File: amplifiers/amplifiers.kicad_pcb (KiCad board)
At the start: 2 copper layers, 4 parts, among them J1 Conn_01x03_Pin, J2 Conn_01x02_Pin, J3 Conn_01x03_Pin, U1 ADA4898-2

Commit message: Finishes version 0.1 of amplifier module board
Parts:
- moved J3 6.73 mm to (151.0, 88.9)
- moved U1 5.35 mm to (143.9, 91.9)
- moved J2 4.92 mm to (142.7, 86.0)
- moved J1 4.61 mm to (137.0, 94.0)
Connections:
- U1 pad 5: Net-(J3-Pin_2) -> Net-(J3-Pin_3)
- U1 pad 6: Net-(J3-Pin_3) -> Net-(J3-Pin_2)
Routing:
- net Net-(J2-Pin_2): track 0.00 -> 9.89 mm
- net VEE: track 0.00 -> 8.55 mm
- net VDD: track 0.00 -> 7.54 mm, vias 0 -> 1
- net Net-(J1-Pin_3): track 0.00 -> 5.98 mm
- net Net-(J3-Pin_2): track 0.00 -> 5.07 mm
- net Net-(J1-Pin_2): track 0.00 -> 4.87 mm
- net Net-(J3-Pin_3): track 0.00 -> 4.70 mm
- net Net-(J2-Pin_1): track 0.00 -> 4.54 mm
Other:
- board outline added: 18 x 14 mm
- board text added: "+In1"
- board text added: "+In2"
- board text added: "+Vs"
- board text added: "-In1"
- board text added: "-In2"
- board text added: "-Vs"
- board text added: "Analog Amplifier"
- board text added: "Vo1"
- board text added: "Vo2"
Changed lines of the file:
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@@
   )
   (paper "A4")
+  (title_block
+    (title "Analog Amplifier Module Board PCB")
+    (date "2024-02-07")
+    (rev "0.1")
+    (company "Carlos Craveiro")
+    (comment 1 "Part of the Eibstein-Boltzmann Project")
+  )
   (layers
     (0 "F.Cu" signal)
@@
   (net 8 "Net-(J3-Pin_3)")
   (footprint "Package_SO:SOIC-8-1EP_3.9x4.9mm_P1.27mm_EP2.41x3.81mm" (layer "F.Cu")
-    (at 148.525 94.595)
+    (at 143.9 91.905)
     (descr "SOIC, 8 Pin (https://www.analog.com/media/en/technical-documentation/data-sheets/ada4898-1_4898-2.pdf#page=29), generated with kicad-footprint-generator ipc_gullwing_generator.py")
     (tags "SOIC SO")
@@
     (attr smd)
     (fp_text reference "U1" (at 0 -3.4) (layer "F.SilkS")
-        (effects (font (size 1 1) (thickness 0.15)))
+        (effects (font (size 1 1) (thickness 0.2) bold))
     )
     (fp_text value "ADA4898-2" (at 0 3.4) (layer "F.Fab")
@@
       (net 1 "VEE") (pinfunction "V-") (pintype "power_in"))
     (pad "5" smd roundrect (at 2.475 1.905) (size 1.95 0.6) (layers "F.Cu" "F.Paste" "F.Mask") (roundrect_rratio 0.25)
-      (net 7 "Net-(J3-Pin_2)") (pinfunction "+") (pintype "input"))
+      (net 8 "Net-(J3-Pin_3)") (pinfunction "+") (pintype "input"))
     (pad "6" smd roundrect (at 2.475 0.635) (size 1.95 0.6) (layers "F.Cu" "F.Paste" "F.Mask") (roundrect_rratio 0.25)
-      (net 8 "Net-(J3-Pin_3)") (pinfunction "-") (pintype "input"))
+      (net 7 "Net-(J3-Pin_2)") (pinfunction "-") (pintype "input"))
     (pad "7" smd roundrect (at 2.475 -0.635) (size 1.95 0.6) (layers "F.Cu" "F.Paste" "F.Mask") (roundrect_rratio 0.25)
       (net 5 "Net-(J2-Pin_2)") (pintype "output"))
@@
       (rotate (xyz 0 0 0))
     )
+    (model "/home/coveiro/Documents/Zedney/einstein-boltzmann/tension-multiplier/R_8_ADI.step"
+      (offset (xyz 0 0 0))
+      (scale (xyz 1 1 1))
+      (rotate (xyz 0 0 0))
+    )
   )
   (footprint "Connector_PinHeader_2.54mm:PinHeader_1x03_P2.54mm_Vertical" (layer "B.Cu")
-    (at 157 91.96 180)
+    (at 151 88.92 180)
     (descr "Through hole straight pin header, 1x03, 2.54mm pitch, single row")
     (tags "Through hole pin header THT 1x03 2.54mm single row")
@@
     (property "ki_keywords" "connector")
     (attr through_hole)
-    (fp_text reference "J3" (at 0 2.33) (layer "B.SilkS")
-        (effects (font (size 1 1) (thickness 0.15)) (justify mirror))
+    (fp_text reference "J3" (at 0 -7.58) (layer "B.SilkS")
+        (effects (font (size 1 1) (thickness 0.2) bold) (justify mirror))
     )
     (fp_text value "Conn_01x03_Pin" (at 0 -7.41) (layer "B.Fab")
@@
   )
   (footprint "Connector_PinHeader_2.54mm:PinHeader_1x03_P2.54mm_Vertical" (layer "B.Cu")
-    (at 140 97.5)
+    (at 137 94)
     (descr "Through hole straight pin header, 1x03, 2.54mm pitch, single row")
     (tags "Through hole pin header THT 1x03 2.54mm single row")
@@
     (attr through_hole)
     (fp_text reference "J1" (at 0 2.33) (layer "B.SilkS")
-        (effects (font (size 1 1) (thickness 0.15)) (justify mirror))
+        (effects (font (size 1 1) (thickness 0.2) bold) (justify mirror))
     )
     (fp_text value "Conn_01x03_Pin" (at 0 -7.41) (layer "B.Fab")
@@
   )
   (footprint "Connector_PinHeader_2.54mm:PinHeader_1x02_P2.54mm_Vertical" (layer "B.Cu")
-    (at 146.96 88.5 -90)
+    (at 142.725 86 -90)
     (descr "Through hole straight pin header, 1x02, 2.54mm pitch, single row")
     (tags "Through hole pin header THT 1x02 2.54mm single row")
@@
     (property "ki_keywords" "connector")
     (attr through_hole)
-    (fp_text reference "J2" (at 0 2.33 90) (layer "B.SilkS")
-        (effects (font (size 1 1) (thickness 0.15)) (justify mirror))
+    (fp_text reference "J2" (at 2.5 -1.275) (layer "B.SilkS")
+        (effects (font (size 1 1) (thickness 0.2) bold) (justify mirror))
     )
     (fp_text value "Conn_01x02_Pin" (at 0 -4.87 90) (layer "B.Fab")
@@
     )
   )
+  (gr_arc (start 152 84) (mid 152.707107 84.292893) (end 153 85)
+    (stroke (width 0.1) (type default)) (layer "Edge.Cuts"))
+  (gr_arc (start 136 98) (mid 135.292893 97.707107) (end 135 97)
+    (stroke (width 0.1) (type default)) (layer "Edge.Cuts"))
+  (gr_arc (start 135 85) (mid 135.292893 84.292893) (end 136 84)
+    (stroke (width 0.1) (type default)) (layer "Edge.Cuts"))
+  (gr_line (start 136 98) (end 152 98)
+    (stroke (width 0.1) (type default)) (layer "Edge.Cuts"))
+  (gr_arc (start 153 97) (mid 152.707107 97.707107) (end 152 98)
+    (stroke (width 0.1) (type default)) (layer "Edge.Cuts"))
+  (gr_line (start 153 85) (end 153 97)
+    (stroke (width 0.1) (type default)) (layer "Edge.Cuts"))
+  (gr_line (start 136 84) (end 152 84)
+    (stroke (width 0.1) (type default)) (layer "Edge.Cuts"))
+  (gr_line (start 135 85) (end 135 97)
+    (stroke (width 0.1) (type default)) (layer "Edge.Cuts"))
+  (gr_text "+In1" (at 142.5 92) (layer "B.SilkS")
+    (effects (font (size 1 1) (thickness 0.2) bold) (justify left bottom mirror))
+  )
+  (gr_text "Vo1" (at 141 86.5) (layer "B.SilkS")
+    (effects (font (size 1 1) (thickness 0.2) bold) (justify left bottom mirror))
+  )
+  (gr_text "+Vs" (at 149.5 89.5) (layer "B.SilkS")
+    (effects (font (size 1 1) (thickness 0.2) bold) (justify left bottom mirror))
+  )
+  (gr_text "-In2" (at 149.5 92) (layer "B.SilkS")
+    (effects (font (size 1 1) (thickness 0.2) bold) (justify left bottom mirror))
+  )
+  (gr_text "-Vs" (at 142 94.5) (layer "B.SilkS")
+    (effects (font (size 1 1) (thickness 0.2) bold) (justify left bottom mirror))
+  )
+  (gr_text "+In2" (at 149.5 94.5) (layer "B.SilkS")
+    (effects (font (size 1 1) (thickness 0.2) bold) (justify left bottom mirror))
+  )
+  (gr_text "Vo2" (at 150 86.5) (layer "B.SilkS")
+    (effects (font (size 1 1) (thickness 0.2) bold) (justify left bottom mirror))
+  )
+  (gr_text "-In1" (at 142.5 89.5) (layer "B.SilkS")
+    (effects (font (size 1 1) (thickness 0.2) bold) (justify left bottom mirror))
+  )
+  (gr_text "Analog Amplifier" (at 138 97) (layer "F.SilkS")
+    (effects (font (size 1 1) (thickness 0.2) bold) (justify left bottom))
+  )
+  (segment (start 141.425 93.81) (end 137.19 93.81) (width 0.5) (layer "F.Cu") (net 1))
+  (segment (start 143.9 91.905) (end 144 92.005) (width 0.5) (layer "F.Cu") (net 1))
+  (segment (start 144 93) (end 143.19 93.81) (width 0.5) (layer "F.Cu") (net 1))
+  (segment (start 144 92.005) (end 144 93) (width 0.5) (layer "F.Cu") (net 1))
+  (segment (start 143.19 93.81) (end 141.425 93.81) (width 0.5) (layer "F.Cu") (net 1))
+  (segment (start 137.19 93.81) (end 137 94) (width 0.5) (layer "F.Cu") (net 1))
+  (segment (start 138.46 91.46) (end 137 91.46) (width 0.3) (layer "F.Cu") (net 2))
+  (segment (start 139.54 92.54) (end 138.46 91.46) (width 0.3) (layer "F.Cu") (net 2))
+  (segment (start 141.425 92.54) (end 139.54 92.54) (width 0.3) (layer "F.Cu") (net 2))
+  (segment (start 138.42 88.92) (end 139 89.5) (width 0.3) (layer "F.Cu") (net 3))
+  (segment (start 139.77 91.27) (end 141.425 91.27) (width 0.3) (layer "F.Cu") (net 3))
+  (segment (start 139 90.5) (end 139.77 91.27) (width 0.3) (layer "F.Cu") (net 3))
+  (segment (start 139 89.5) (end 139 90.5) (width 0.3) (layer "F.Cu") (net 3))
+  (segment (start 137 88.92) (end 138.42 88.92) (width 0.3) (layer "F.Cu") (net 3))
+  (segment (start 142.725 86) (end 142.725 88.7) (width 0.3) (layer "F.Cu") (net 4))
+  (segment (start 142.725 88.7) (end 141.425 90) (width 0.3) (layer "F.Cu") (net 4))
+  (segment (start 148.23 91.27) (end 148.5 91) (width 0.3) (layer "F.Cu") (net 5))
+  (segment (start 148.5 87) (end 147.5 86) (width 0.3) (layer "F.Cu") (net 5))
+  (segment (start 146.375 91.27) (end 148.23 91.27) (width 0.3) (layer "F.Cu") (net 5))
+  (segment (start 148.5 91) (end 148.5 87) (width 0.3) (layer "F.Cu") (net 5))
+  (segment (start 147.5 86) (end 145.265 86) (width 0.3) (layer "F.Cu") (net 5))
+  (segment (start 146.375 89.375) (end 146.375 90) (width 0.5) (layer "F.Cu") (net 6))
+  (segment (start 145.5 88.5) (end 146.375 89.375) (width 0.5) (layer "F.Cu") (net 6))
+  (via (at 145.5 88.5) (size 0.8) (drill 0.4) (layers "F.Cu" "B.Cu") (net 6))
+  (segment (start 145.5 88.5) (end 150.58 88.5) (width 0.5) (layer "B.Cu") (net 6))
+  (segment (start 150.58 88.5) (end 151 88.92) (width 0.5) (layer "B.Cu") (net 6))
+  (segment (start 149.54 91.46) (end 151 91.46) (width 0.3) (layer "F.Cu") (net 7))
+  (segment (start 146.375 92.54) (end 148.46 92.54) (width 0.3) (layer "F.Cu") (net 7))
+  (segment (start 148.46 92.54) (end 149.54 91.46) (width 0.3) (layer "F.Cu") (net 7))
+  (segment (start 150.81 93.81) (end 151 94) (width 0.3) (layer "F.Cu") (net 8))
+  (segment (start 146.375 93.81) (end 150.81 93.81) (width 0.3) (layer "F.Cu") (net 8))
 )

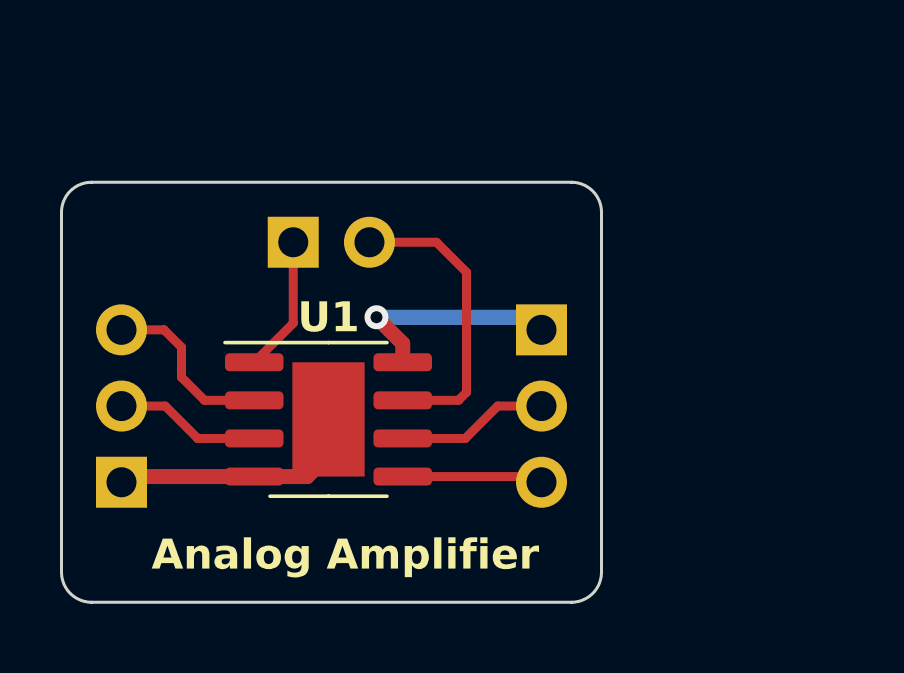
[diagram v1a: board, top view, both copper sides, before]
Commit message: Refactors modules pcblayout to cosmetic purposes
Also, refactors Amplifiers moduleboard to include a VEE plane
(powerplane).
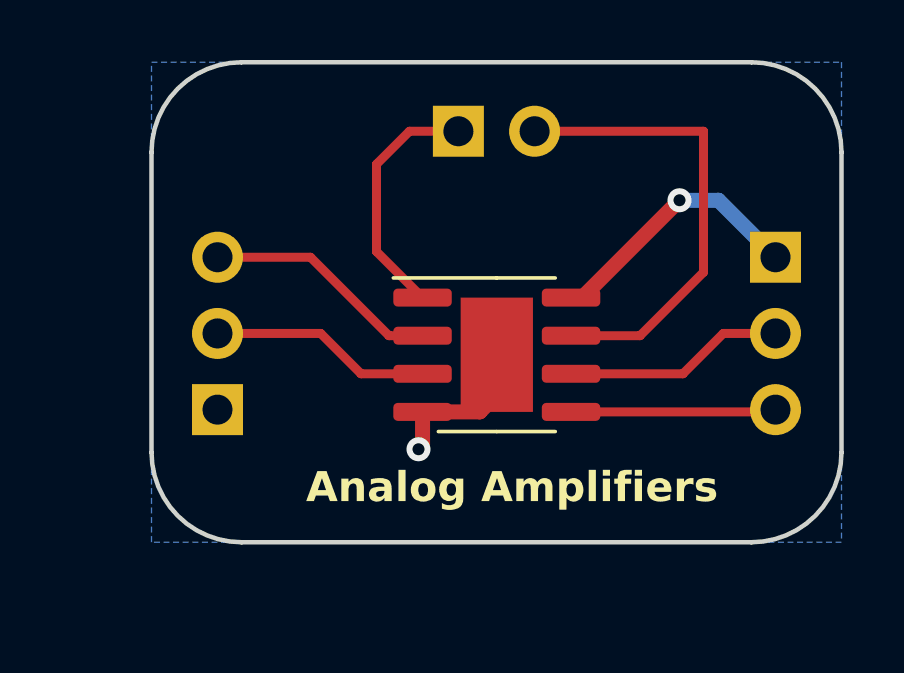
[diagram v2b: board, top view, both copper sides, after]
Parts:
- moved J3 8.17 mm to (158.8, 86.5)
- moved J2 6.63 mm to (148.2, 82.3)
- moved U1 6.01 mm to (149.5, 89.8)
- moved J1 4.01 mm to (140.2, 91.6)
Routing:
- net Net-(J2-Pin_2): track 9.89 -> 15.6 mm
- net Net-(J2-Pin_1): track 4.54 -> 8.27 mm
- net VEE: track 8.55 -> 5.49 mm, vias 0 -> 1
- net Net-(J1-Pin_2): track 4.87 -> 7.39 mm
- net Net-(J3-Pin_2): track 5.07 -> 7.37 mm
- net Net-(J3-Pin_3): track 4.70 -> 6.85 mm
- net Net-(J1-Pin_3): track 5.98 -> 7.92 mm
- net VDD: track 7.54 -> 8.95 mm
- added copper zone on B.Cu, net VEE
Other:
- board size 18 x 14 mm -> 23 x 16 mm
- board text added: "Analog Amplifiers"
- board text removed: "Analog Amplifier"

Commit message: Add JLCPCB serial number to the module pcbs
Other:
- board text added: "JLCJLCJLCJLC"
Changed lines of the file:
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@@
     (effects (font (size 1 1) (thickness 0.2) bold) (justify left bottom mirror))
+  )
+  (gr_text "JLCJLCJLCJLC" (at 153.8 94.8) (layer "B.SilkS")
+    (effects (font (size 0.8 0.8) (thickness 0.15)) (justify left bottom mirror))
   )
   (gr_text "-Vs" (at 145 92.25) (layer "B.SilkS")

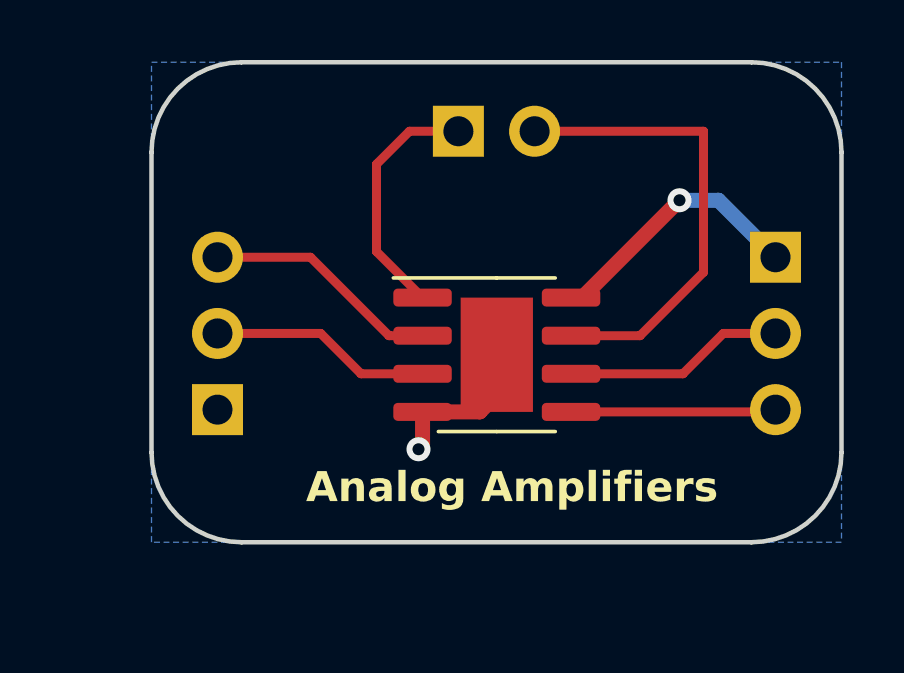
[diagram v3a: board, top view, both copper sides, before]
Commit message: Modifies auxiliary boards
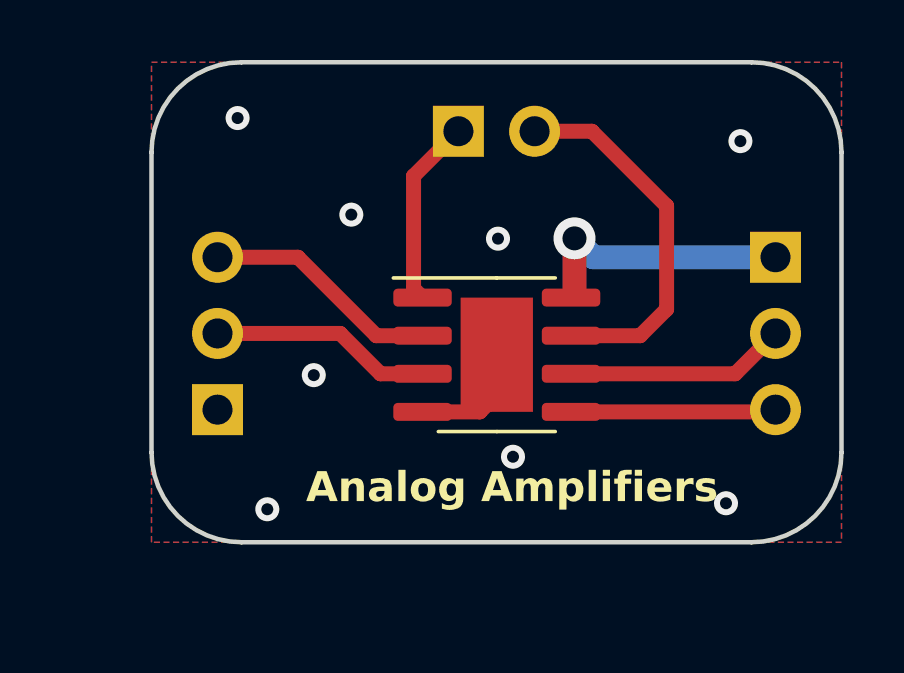
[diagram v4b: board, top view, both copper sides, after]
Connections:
- net VDD renamed +9V
- net VEE renamed -9V
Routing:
- net Net-(J2-Pin_2): track 15.6 -> 12.4 mm
- net Net-(J2-Pin_1): track 8.27 -> 6.29 mm
- net -9V: track 5.49 -> 4.19 mm, vias 1 -> 8
- added copper zone on F.Cu, net -9V
